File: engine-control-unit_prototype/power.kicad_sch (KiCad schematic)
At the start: 90 parts, among them IC1 TPS259573DSGR, J17 2S_18650, J30 EXT_BATT, U10 TPS55285, U11 LT3042xMSE, U13 INA219AxD, U14 LT3042xMSE, U6 INA219AxD, U8 INA219AxD, U9 TPS55285

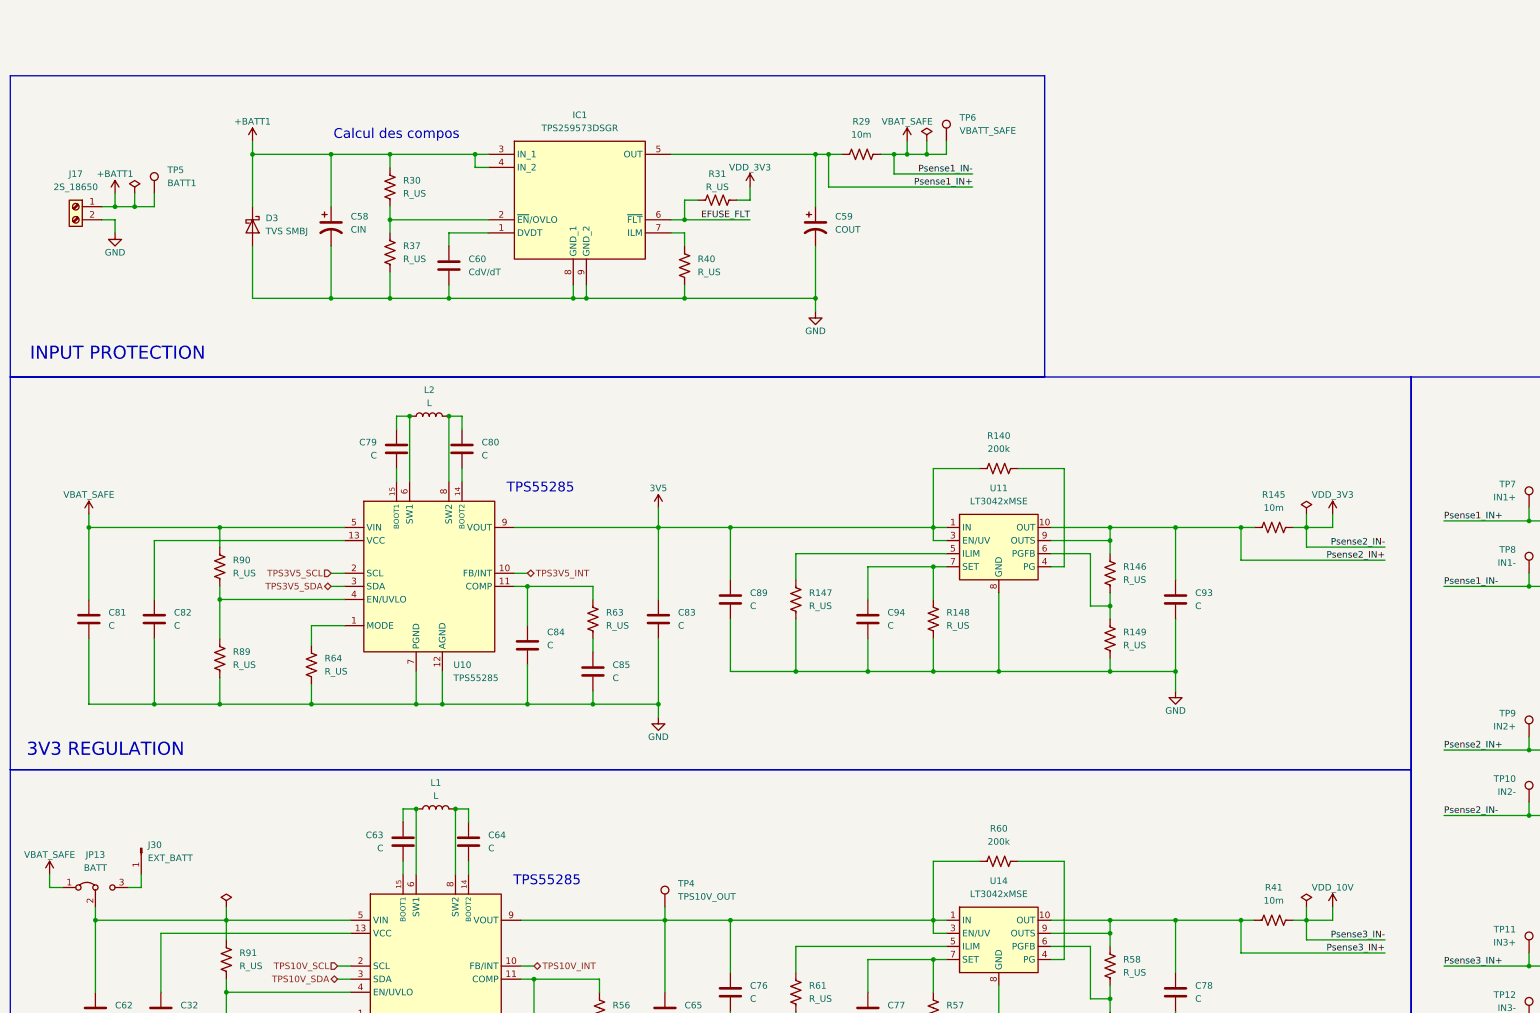
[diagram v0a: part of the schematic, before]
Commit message: Added Control page Revisited power tree (VDDA_3V3 and VDD_3V3) Bunch of other fixes
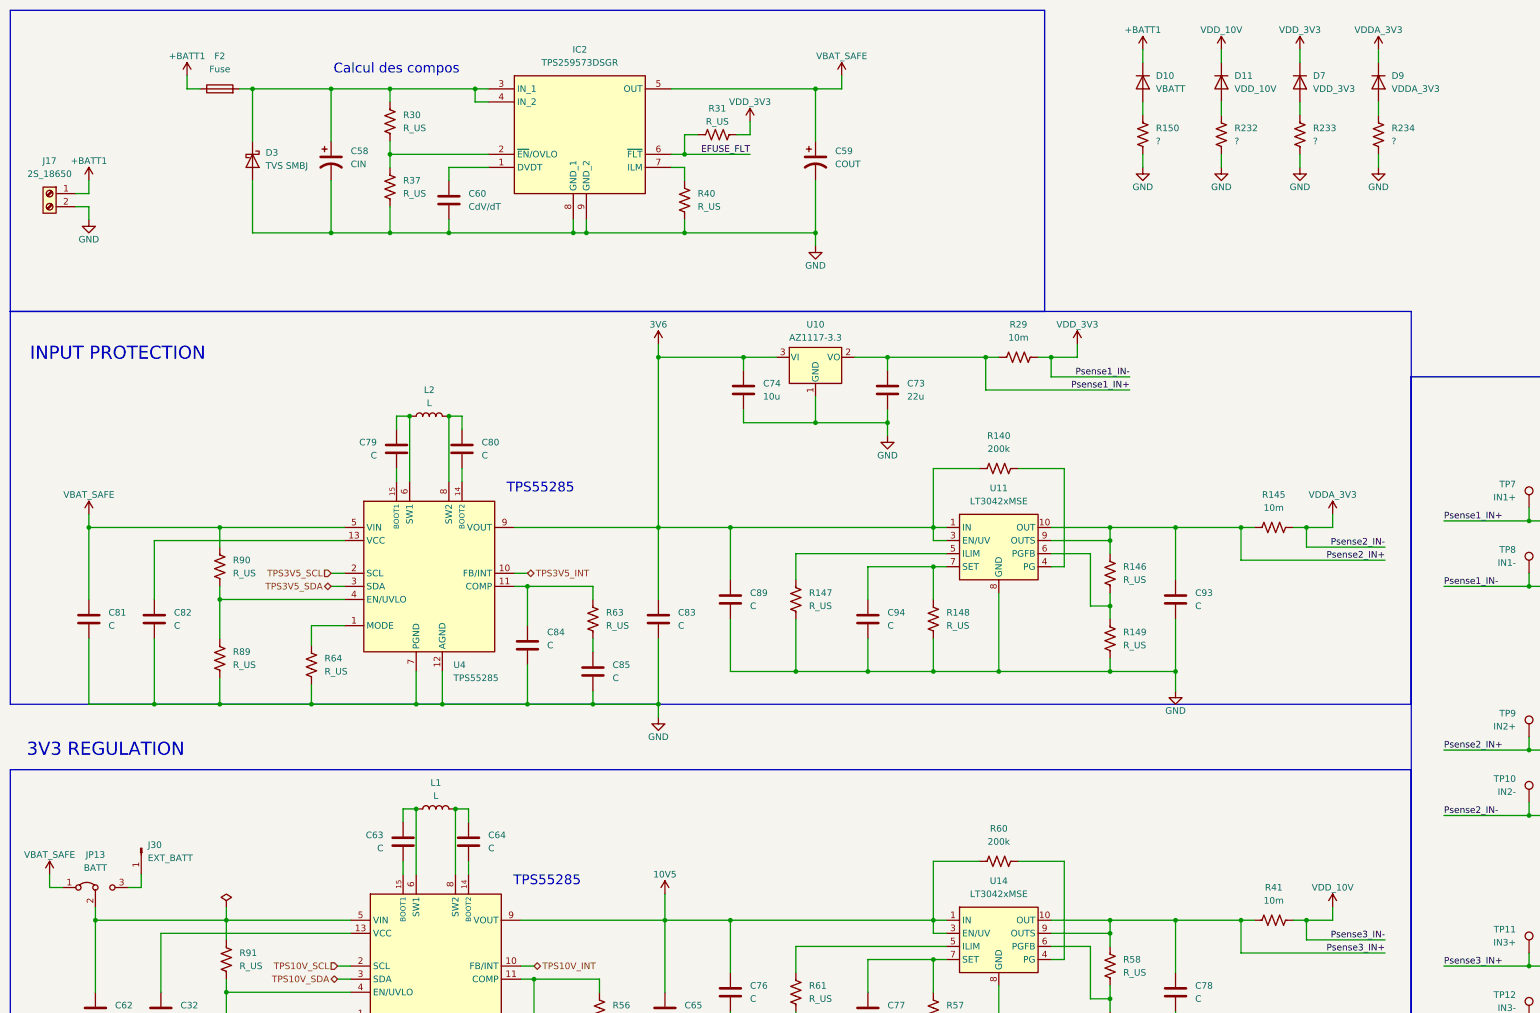
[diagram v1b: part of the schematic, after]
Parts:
- removed IC1: TPS259573DSGR, SON50P200X200X80-9N, symbol TPS259573DSGR:TPS259573DSGR
- removed TP4: TPS10V_OUT, symbol Connector:TestPoint
- removed TP5: BATT1, symbol Connector:TestPoint
- removed TP6: VBATT_SAFE, symbol Connector:TestPoint
- removed U10: TPS55285, symbol SiriusLib:TPS55285
- added C73: 22u, Capacitor_SMD:C_0603_1608Metric, symbol Device:C
- added C74: 10u, Capacitor_SMD:C_0603_1608Metric, symbol Device:C
- added D10: VBATT, symbol Device:D
- added D11: VDD_10V, symbol Device:D
- added D7: VDD_3V3, symbol Device:D
- added D9: VDDA_3V3, symbol Device:D
- added F2: Fuse, symbol Device:Fuse
- added IC2: TPS259573DSGR, SON50P200X200X80-9N, symbol TPS259573DSGR:TPS259573DSGR
- added R150, R232, R233, R234: ?, Resistor_SMD:R_0603_1608Metric, symbol Device:R_US
- added U10: AZ1117-3.3, symbol Regulator_Linear:AZ1117-3.3
- added U4: TPS55285, symbol SiriusLib:TPS55285
- C32, C40, C41, C53, C54, C55, C56, C57, C60, C62, C63, C64, C65, C66, C75, C76, C77, C78, C79, C80, C81, C82, C83, C84, C85, C89, C93, C94: footprint (none) -> Capacitor_SMD:C_0603_1608Metric
- R100, R101, R102, R97, R98, R99: footprint (none) -> Resistor_SMD:R_0201_0603Metric
- R146, R147, R148, R149, R22, R23, R25, R26, R27, R28, R30, R31, R37, R40, R55, R56, R57, R58, R59, R61, R63, R64, R89, R90, R91, R92: footprint (none) -> Resistor_SMD:R_0603_1608Metric
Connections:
- net +BATT1: now also D10.1 (K), F2.1; no longer C58.1, D3.1 (K), R30.1
- net EFUSE_FLT: now also IC2.6 (~{FLT})
- net GND: now also C73.2, C74.2, IC2.8 (GND_1), IC2.9 (GND_2), R150.2, R232.2, R233.2, R234.2, U10.1 (GND), U4.12 (AGND), U4.7 (PGND)
- net Psense1_IN+: now also C73.1, U10.2 (VO); no longer C59.1
- net TPS3V5_INT: now also U4.10 (FB/INT)
- net TPS3V5_SCL: now also U4.2 (SCL)
- net TPS3V5_SDA: now also U4.3 (SDA)
- net VBAT_SAFE: now also C59.1, IC2.5 (OUT), U4.5 (VIN); no longer R23.2, R29.2, TP8.1
- net VDD_10V: now also D11.1 (K)
- net VDD_3V3: now also R23.2, R29.2, TP8.1, D7.1 (K); no longer R145.2, R26.2, TP10.1
- net at C84.1, R63.1: now also U4.11 (COMP)
- net at R40.1: now also IC2.7 (ILM)
- net at C82.1: now also U4.13 (VCC)
- net at R64.1: now also U4.1 (MODE)
- net at C80.2: now also U4.14 (BOOT2)
- net at C79.2: now also U4.15 (BOOT1)
- net at R89.1, R90.2: now also U4.4 (EN/UVLO)
- net at C79.1, L2.1: now also U4.6 (SW1)
- net at C80.1, L2.2: now also U4.8 (SW2)
- net at R30.2, R37.1: now also IC2.2 (~{EN}/OVLO)
- net 10V5: now reaches C65.1, C76.1, R60.1, U14.1 (IN), U14.2 (IN), U14.3 (EN/UV), U9.9 (VOUT)
- net at C60.1: now also IC2.1 (DVDT)
- net 3V5 renamed 3V6
- net 3V6: now also C74.1, U10.3 (VI), U4.9 (VOUT)
- new net: D7.2 (A), R233.1
- new net: D9.2 (A), R234.1
- new net: C58.1, D3.1 (K), F2.2, IC2.3 (IN_1), IC2.4 (IN_2), R30.1
- new net: D11.2 (A), R232.1
- new net: D10.2 (A), R150.1
- new net VDDA_3V3: D9.1 (K), R145.2, R26.2, TP10.1
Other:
- moved on the sheet: C58, C59, C60, D3, J17, R29, R30, R31, R37, R40

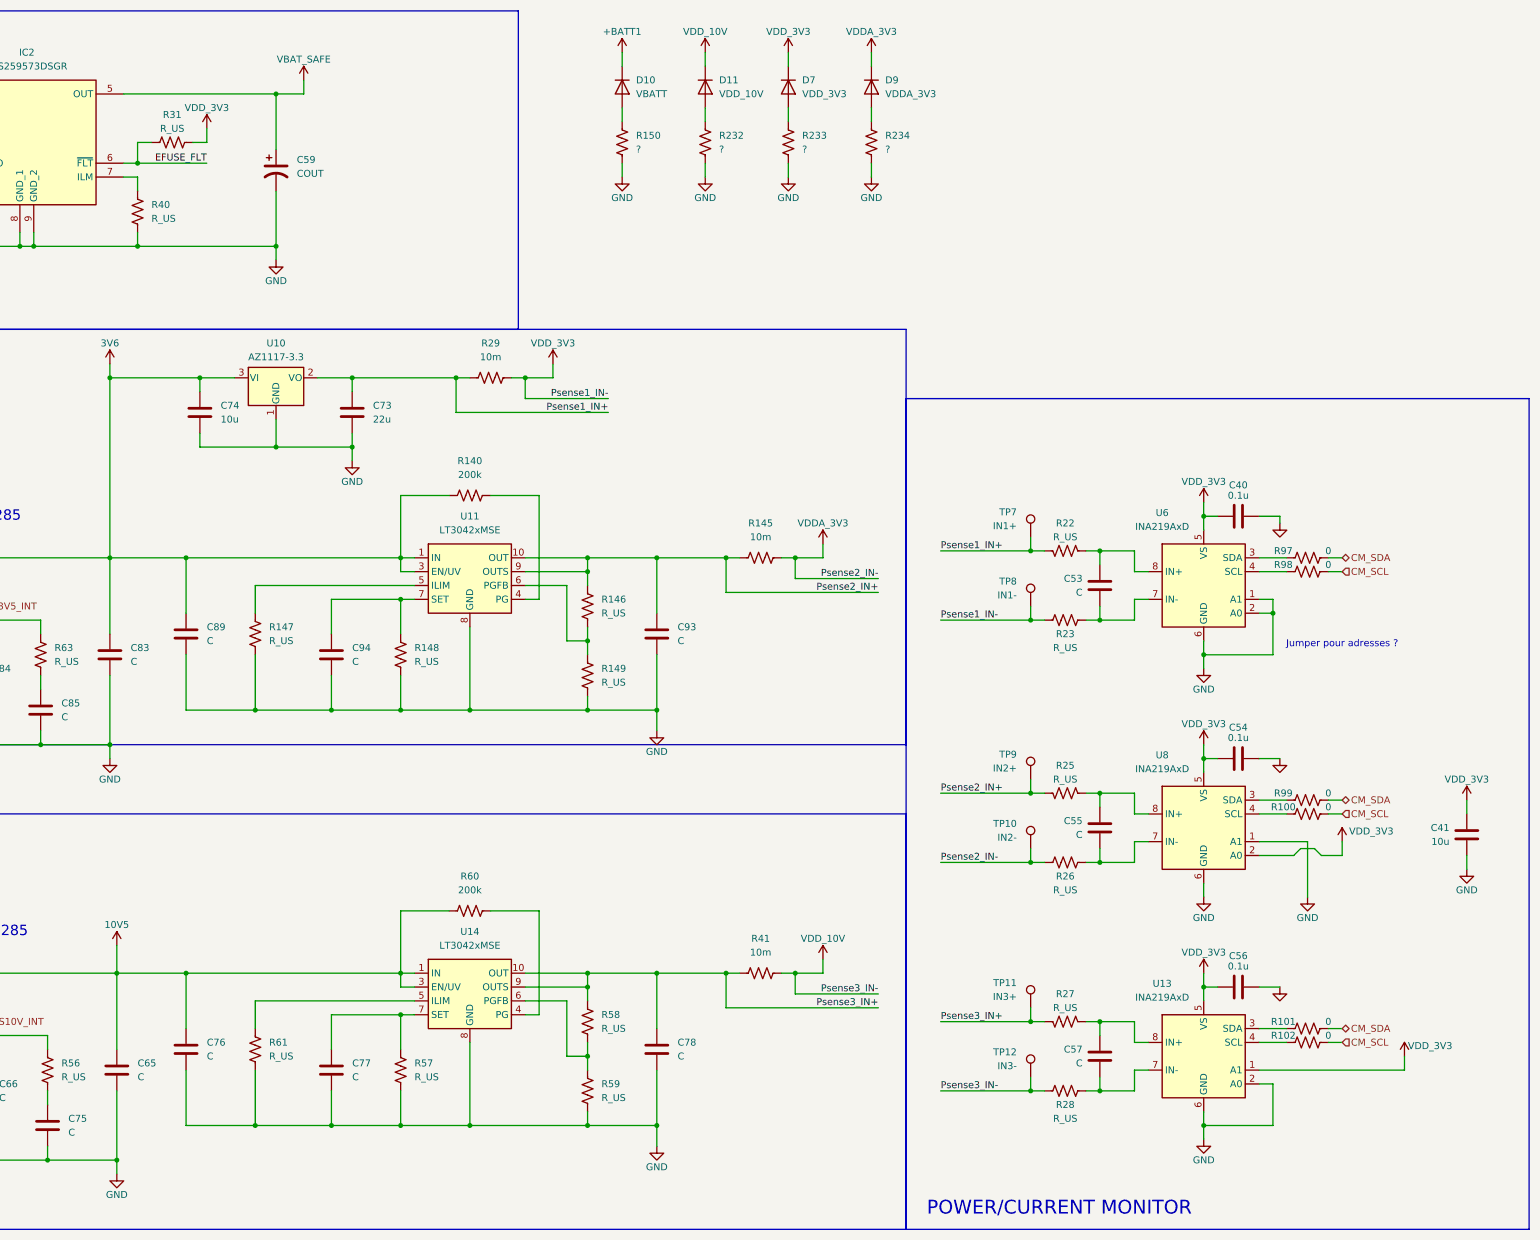
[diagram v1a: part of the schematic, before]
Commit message: Fixed inverted LED diodes (oops) Replaced 3x INA219 with INA3221
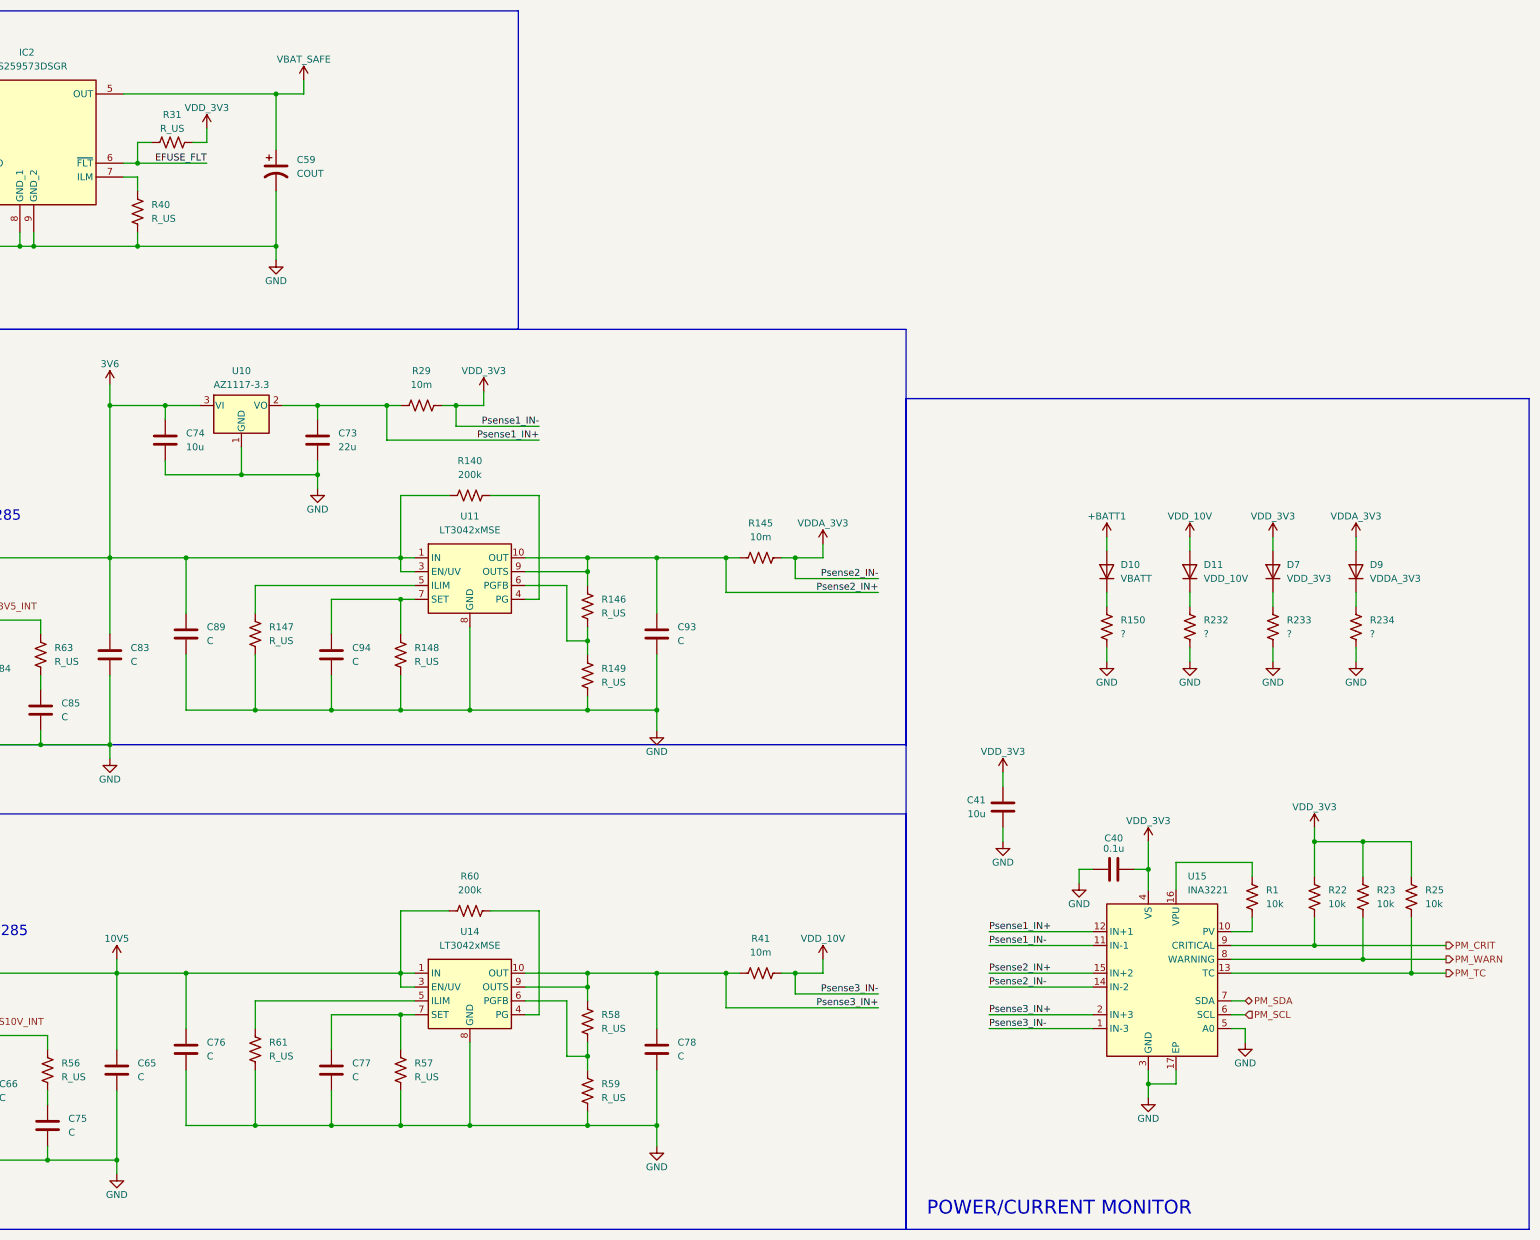
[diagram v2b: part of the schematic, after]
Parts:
- removed C53, C55, C57: C, Capacitor_SMD:C_0603_1608Metric, symbol Device:C
- removed C54, C56: 0.1u, Capacitor_SMD:C_0603_1608Metric, symbol Device:C
- removed R100, R101, R102, R97, R98, R99: 0, Resistor_SMD:R_0201_0603Metric, symbol Device:R_US
- removed R26, R27, R28: R_US, Resistor_SMD:R_0603_1608Metric, symbol Device:R_US
- removed TP10: IN2-, symbol Connector:TestPoint
- removed TP11: IN3+, symbol Connector:TestPoint
- removed TP12: IN3-, symbol Connector:TestPoint
- removed TP7: IN1+, symbol Connector:TestPoint
- removed TP8: IN1-, symbol Connector:TestPoint
- removed TP9: IN2+, symbol Connector:TestPoint
- removed U13, U6, U8: INA219AxD, Package_SO:SOIC-8_3.9x4.9mm_P1.27mm, symbol Sensor_Energy:INA219AxD
- added R1: 10k, symbol Device:R_US
- added U15: INA3221, Package_DFN_QFN:Texas_RGV0016A_VQFN-16-1EP_4x4mm_P0.65mm_EP2.1x2.1mm, symbol Power_Management:INA3221
- R22, R23, R25: value R_US -> 10k; footprint Resistor_SMD:R_0603_1608Metric -> (none)
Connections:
- net +BATT1: now also D10.2 (A); no longer D10.1 (K)
- net GND: now also C40.2, U15.17 (EP), U15.3 (GND), U15.5 (A0); no longer C40.1
- net Psense1_IN+: now also U15.12 (IN+1); no longer R22.2
- net Psense2_IN+: now also U15.15 (IN+2); no longer R25.2
- net Psense3_IN+: now also U15.2 (IN+3)
- net VDDA_3V3: now also D9.2 (A), U15.14 (IN-2); no longer D9.1 (K)
- net VDD_10V: now also D11.2 (A), U15.1 (IN-3); no longer D11.1 (K)
- net VDD_3V3: now also C40.1, D7.2 (A), R22.1, R23.1, R25.1, U15.11 (IN-1), U15.4 (VS); no longer C40.2, D7.1 (K), R23.2
- net at R233.1: now also D7.1 (K); no longer D7.2 (A)
- net at R234.1: now also D9.1 (K); no longer D9.2 (A)
- net at R232.1: now also D11.1 (K); no longer D11.2 (A)
- net at R150.1: now also D10.1 (K); no longer D10.2 (A)
- new net: R1.2, U15.10 (PV)
- new net: R1.1, U15.16 (VPU)
- new net PM_CRIT: R22.2, U15.9 (CRITICAL)
- new net PM_SCL: U15.6 (SCL)
- new net PM_SDA: U15.7 (SDA)
- new net PM_TC: R25.2, U15.13 (TC)
- new net PM_WARN: R23.2, U15.8 (WARNING)
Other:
- note removed: "Jumper pour adresses ?"
- moved on the sheet: C40, C41, C73, C74, D10, D11, D7, D9, R150, R232, R233, R234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

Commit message: Added magnetic encoders Added optional external valve control connector
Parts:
- added R136, R137: 10k, Resistor_SMD:R_0402_1005Metric, symbol Device:R_US
- added R147, R148, R160, R161: 1k, Resistor_SMD:R_0402_1005Metric, symbol Device:R_US
- renumbered C40 to C30, C41 to C31, C58 to C32, C59 to C33, C60 to C34, C74 to C35, C73 to C36, C79 to C37, C80 to C38, C81 to C39, C82 to C40, C83 to C41, C89 to C42, C93 to C43, C84 to C44, C94 to C45, C85 to C46, C63 to C47, C64 to C48, C76 to C49, C78 to C50, C62 to C51, C32 to C52, C65 to C53, C77 to C54, C66 to C55, C75 to C56, D10 to D2, D11 to D3, D7 to D4, D9 to D5, D3 to D6, F2 to F1, IC2 to IC1, J17 to J8, J30 to J9, JP13 to JP1, L2 to L1, L1 to L2, R1 to R132, R22 to R133, R23 to R134, R25 to R135, R30 to R138, R31 to R139, R150 to R140, R232 to R141, R233 to R142, R234 to R143, R37 to R144, R40 to R145, R29 to R146, R140 to R149, R145 to R150, R90 to R151, R146 to R152, R63 to R153, R147 to R154, R89 to R155, R148 to R156, R64 to R157, R149 to R158, R60 to R159, R41 to R162, R91 to R163, R58 to R164, R61 to R165, R56 to R166, R57 to R167, R59 to R168, R92 to R169, R55 to R170, U15 to U2, U10 to U3, U11 to U5, U9 to U6, U14 to U7
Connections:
- net PM_SCL: now also R137.2
- net PM_SDA: now also R136.2
- net TPS10V_SCL: now also R160.2
- net TPS10V_SDA: now also R161.2
- net TPS3V5_SCL: now also R147.2
- net TPS3V5_SDA: now also R148.2
- net VDD_3V3: now also R136.1, R137.1, R147.1, R148.1, R160.1, R161.1
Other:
- moved on the sheet: C30, C31, C32, C33, C34, C35, C36, C37, C38, C41, C42, C43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
